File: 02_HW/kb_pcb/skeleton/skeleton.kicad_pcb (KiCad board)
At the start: 2 copper layers, 67 parts, among them J1 Adafruit_Feather_16_pin, J2 Adafruit_feather_12_pin, SW1 SW_Push, SW10 SW_Push, SW11 SW_Push, SW12 SW_Push, SW13 SW_Push, SW14 SW_Push, SW15 SW_Push, SW16 SW_Push, SW17 SW_Push, SW18 SW_Push, SW19 SW_Push, SW2 SW_Push, SW20 SW_Push, SW21 SW_Push, SW22 SW_Push, SW23 SW_Push, SW24 SW_Push, SW25 SW_Push, SW26 SW_Push, SW27 SW_Push, SW28 SW_Push, SW29 SW_Push, SW3 SW_Push, SW30 SW_Push, SW4 SW_Push, SW5 SW_Push, SW6 SW_Push, SW7 SW_Push, SW8 SW_Push, SW9 SW_Push

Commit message: Organized key layout
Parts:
- R1, R2, R3, R4, R5: footprint Button_Switch_Keyboard:SW_Cherry_MX_1.00u_PCB -> Resistor_SMD:R_0603_1608Metric
- moved R1 214.0 mm to (265.7, 144.5)
- moved SW4 200.9 mm to (52.1, 58.4)
- moved R2 200.9 mm to (279.2, 140.5)
- moved SW7 178.9 mm to (75.8, 98.5)
- moved SW13 177.2 mm to (97.5, 73.4)
- moved R3 174.4 mm to (243.5, 139.9)
- moved R4 174.4 mm to (243.5, 155.0)
- moved SW6 167.9 mm to (193.3, 137.5)
- moved SW3 158.2 mm to (51.9, 79.0)
- moved SW1 157.0 mm to (193.0, 157.5)
- moved SW14 156.5 mm to (97.5, 53.9)
- moved R5 155.5 mm to (255.7, 137.0)
- moved SW11 120.8 mm to (193.5, 118.0)
- moved SW19 104.6 mm to (119.3, 47.2)
- moved SW12 101.3 mm to (97.3, 93.0)
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
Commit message: Positioned key switches and diodes
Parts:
- moved D4 230.4 mm to (30.9, 64.9), turned to 180 degrees
- moved D3 226.6 mm to (30.9, 83.9), turned to 180 degrees
- moved D2 225.0 mm to (30.9, 103.0), turned to 180 degrees
- moved D10 220.5 mm to (49.9, 45.8), turned to 180 degrees
- moved D9 215.3 mm to (49.9, 64.9), turned to 180 degrees
- moved D8 210.5 mm to (49.9, 83.9), turned to 180 degrees
- moved D15 207.9 mm to (69.0, 45.8), turned to 180 degrees
- moved D7 207.0 mm to (49.9, 103.0), turned to 180 degrees
- moved D14 200.5 mm to (69.0, 64.9), turned to 180 degrees
- moved D13 195.4 mm to (69.0, 83.9), turned to 180 degrees
- moved D12 192.8 mm to (69.0, 103.0), turned to 180 degrees
- moved D20 191.8 mm to (88.0, 45.8), turned to 180 degrees
- moved D19 185.0 mm to (88.0, 64.9), turned to 180 degrees
- moved D18 180.6 mm to (88.0, 83.9), turned to 180 degrees
- moved D17 179.0 mm to (88.0, 103.0), turned to 180 degrees
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
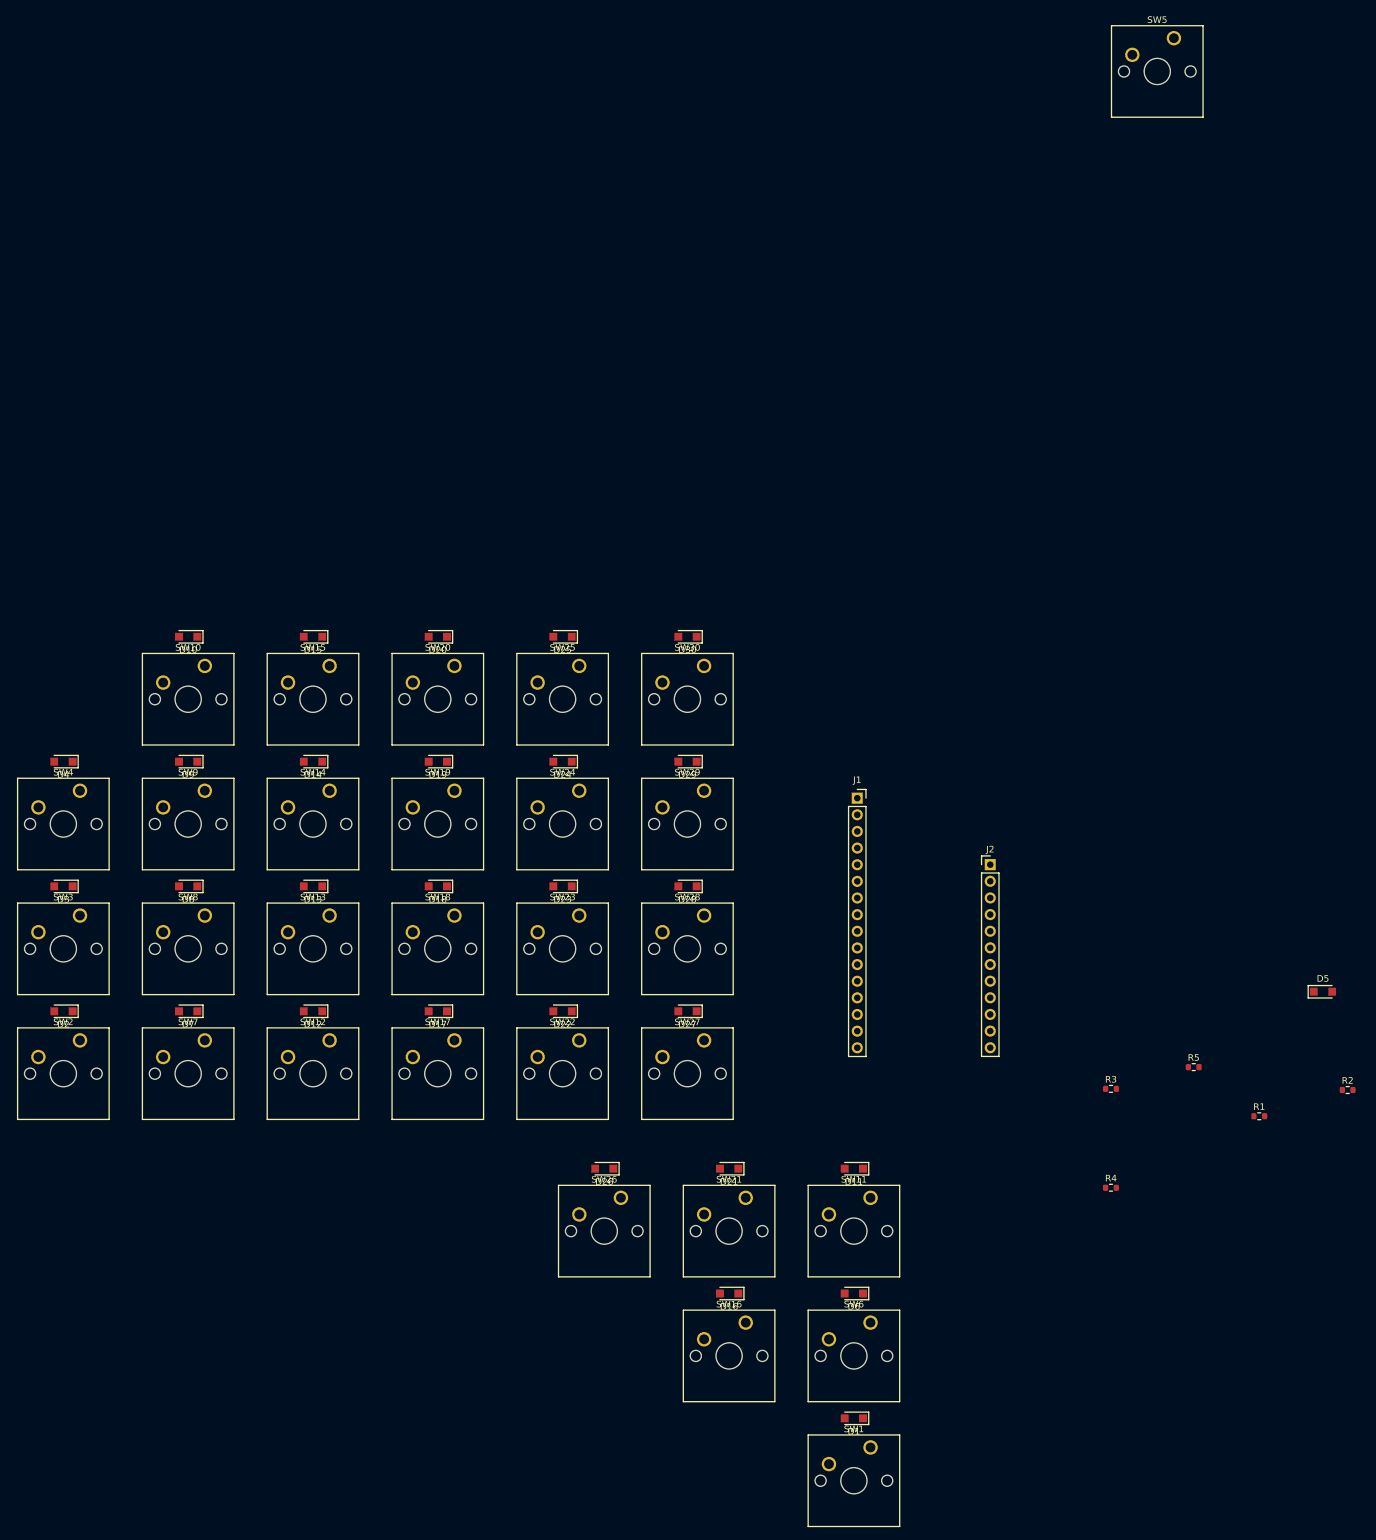
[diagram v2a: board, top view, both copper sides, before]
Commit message: Positioned key switch columns. Began fixing net labels
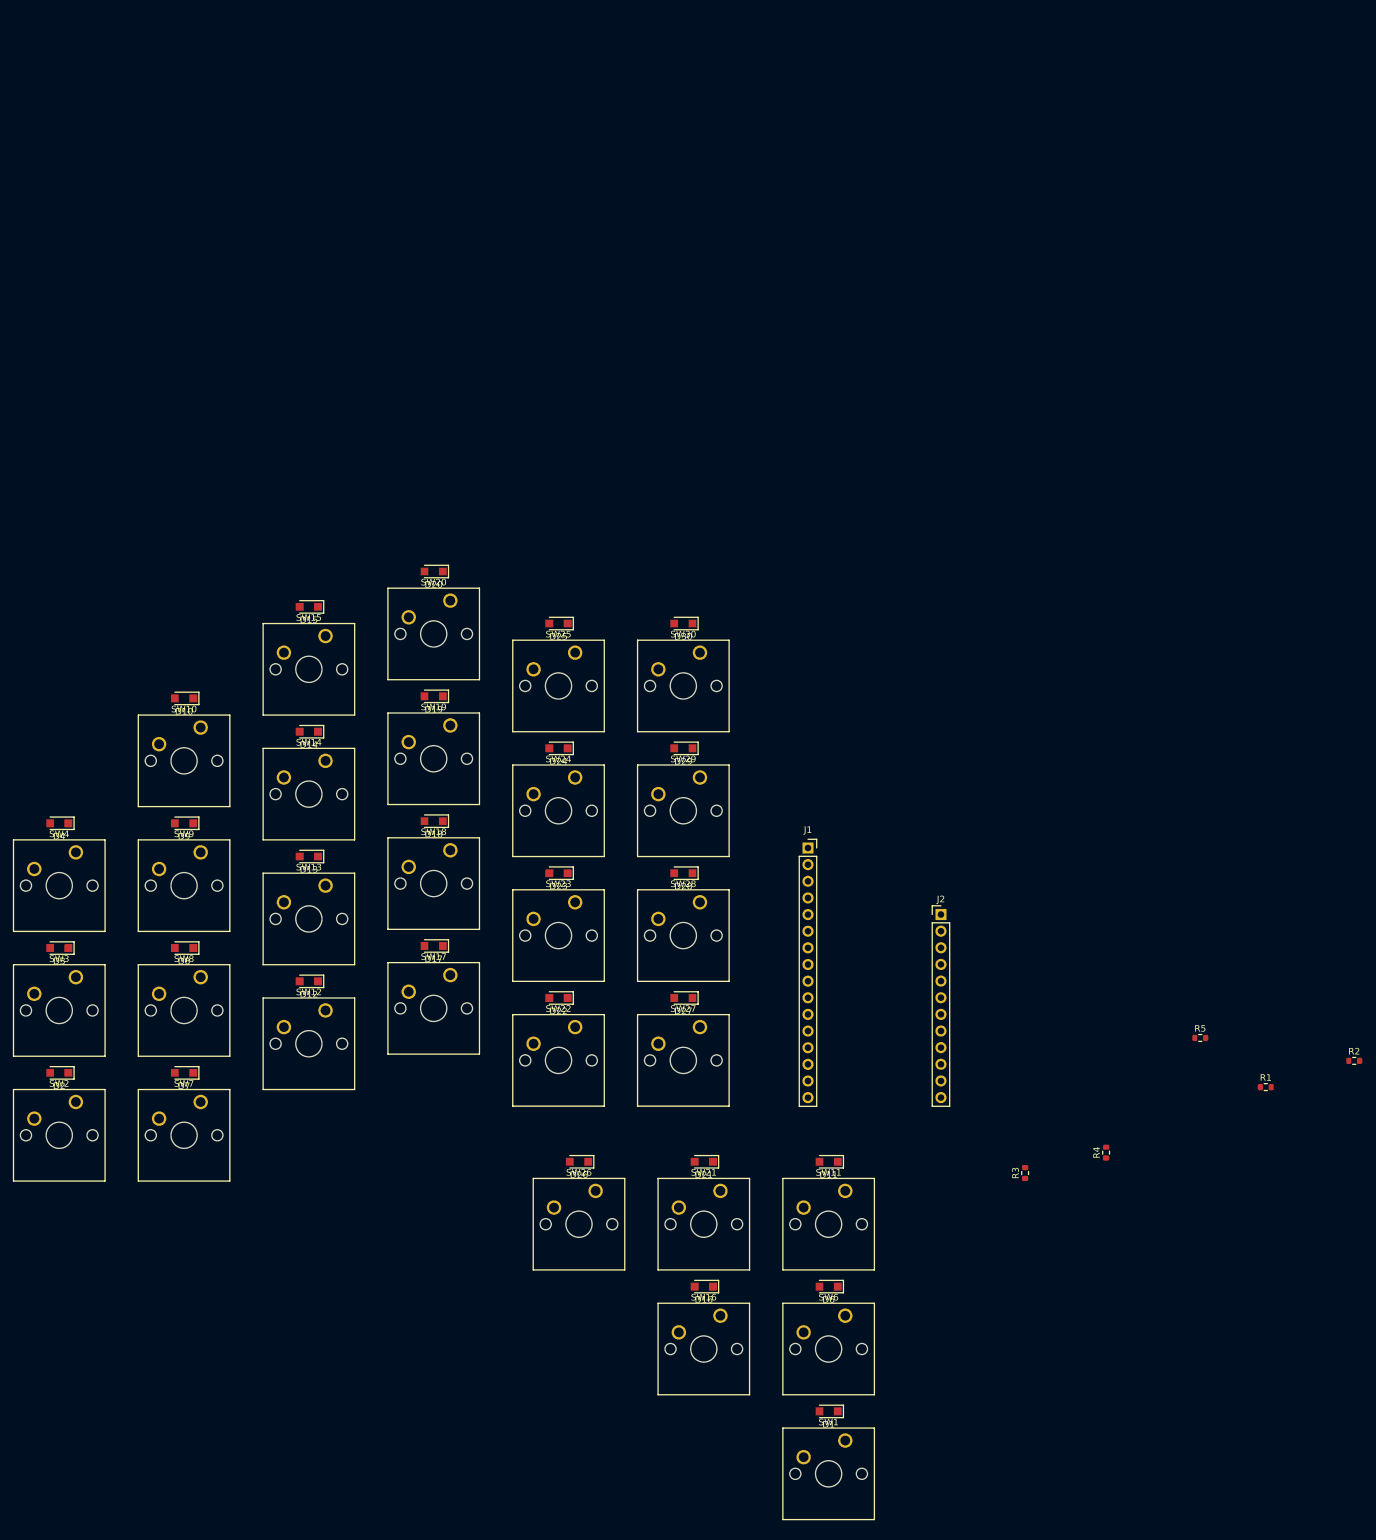
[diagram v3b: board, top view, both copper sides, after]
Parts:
- removed D5: D, Diode_SMD:Nexperia_CFP3_SOD-123W
- removed SW5: SW_Push, Button_Switch_Keyboard:SW_Cherry_MX_1.00u_PCB
- moved R3 18.4 mm to (177.6, 127.7), turned to 90 degrees
- moved J1 10.7 mm to (144.5, 78.1)
- moved J2 10.7 mm to (164.8, 88.2)
- moved D20 9.98 mm to (87.4, 35.9)
- moved SW17 9.98 mm to (89.9, 97.5)
- moved SW18 9.98 mm to (89.9, 78.4)
- moved SW20 9.98 mm to (89.9, 40.3)
- moved D19 9.98 mm to (87.4, 54.9)
- moved D17 9.98 mm to (87.4, 93.0)
- moved D18 9.98 mm to (87.4, 74.0)
- moved SW19 9.98 mm to (89.9, 59.4)
- moved D2 9.43 mm to (30.2, 112.4)
- moved D3 9.43 mm to (30.2, 93.3)
- moved D4 9.43 mm to (30.2, 74.3)
- moved D7 9.43 mm to (49.3, 112.4)
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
